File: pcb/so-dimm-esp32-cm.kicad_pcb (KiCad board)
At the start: 4 copper layers, 67.6 x 31.1 mm, 31 parts, among them IC1 PI4IOE5V9535LEX, IC2 PI4IOE5V9535LEX, J1 SODIMM-200, J2 Debug Connector/DNP, U1 ESP32-S2-SOLO

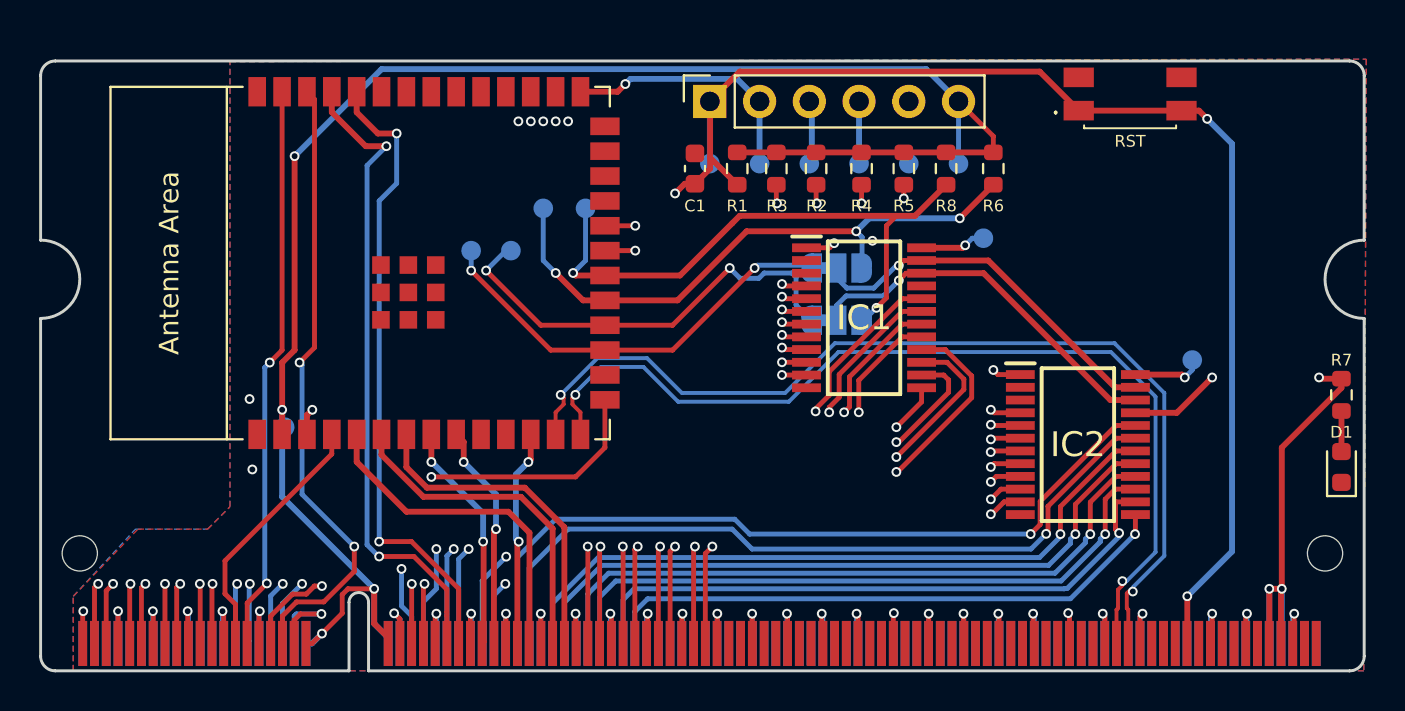
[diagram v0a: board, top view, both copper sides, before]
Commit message: Refactored PCB Layer to have one dedicated GND Layer + rerouted traces + removed debug connector and added IO0 to the SO-DIMM connector + added decoupling caps and delay circuit for ESP32 module
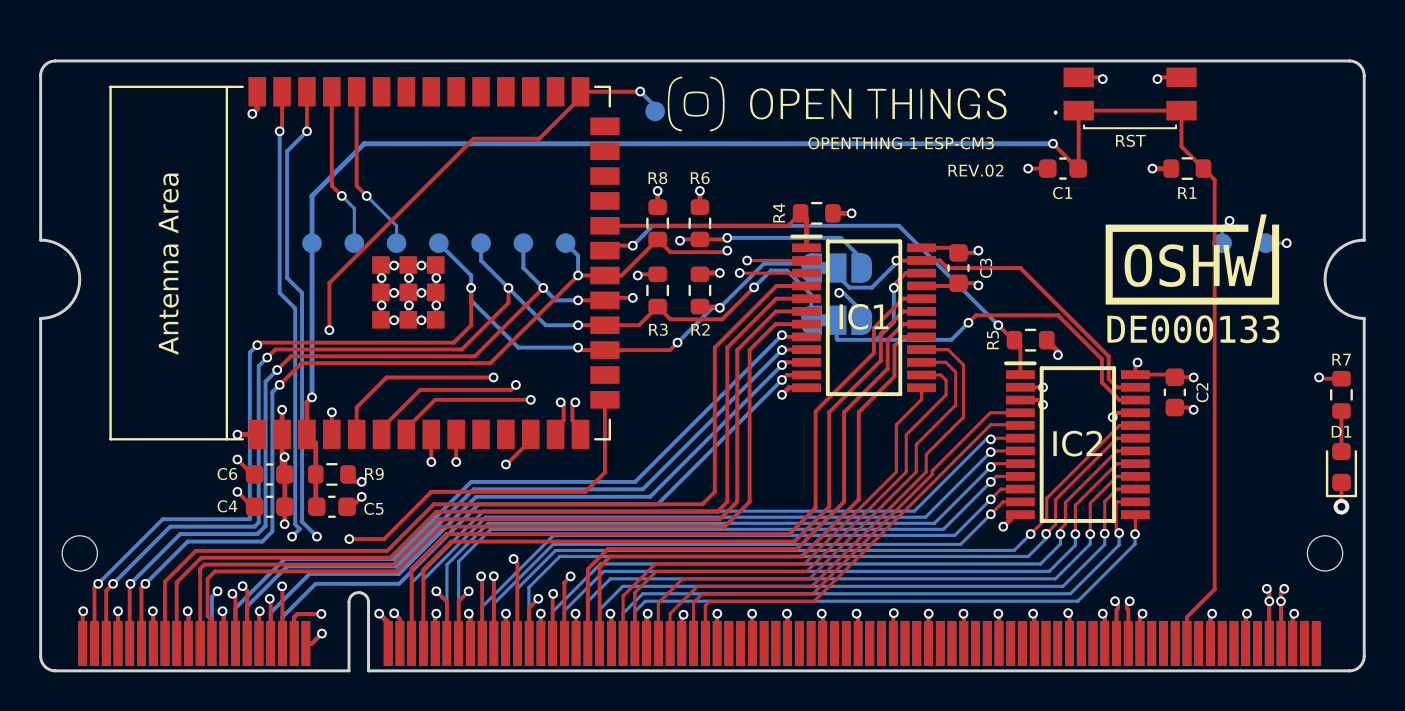
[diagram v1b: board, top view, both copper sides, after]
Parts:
- removed J2: Debug Connector/DNP, Connector_PinSocket_2.54mm:PinSocket_1x06_P2.54mm_Vertical
- removed TP5, TP7, TP9: TP_3V3, TestPoint:TestPoint_Pad_D1.0mm
- added C2: 0.1uF, Capacitor_SMD:C_0603_1608Metric, F.Cu at (173.4, 93.9)
- added C3: 0.1uF, Capacitor_SMD:C_0603_1608Metric, F.Cu at (162.3, 87.5)
- added C4: 10uF, Capacitor_SMD:C_0603_1608Metric, F.Cu at (127.1, 99.7)
- added C5: 1uF, Capacitor_SMD:C_0603_1608Metric, F.Cu at (130.3, 99.7)
- added C6: 0.1uF, Capacitor_SMD:C_0603_1608Metric, F.Cu at (127.1, 98.0)
- added G1: LOGO, LOGO, F.Cu at (156.3, 79.1)
- added G2: LOGO, LOGO, F.Cu at (174.2, 88.3)
- added R9: 10k, Resistor_SMD:R_0603_1608Metric, F.Cu at (130.3, 98.0)
- moved TP8 51.0 mm to (178.0, 86.2)
- moved TP4 26.1 mm to (131.4, 86.2)
- moved R1 23.0 mm to (174.0, 82.4), turned to 180 degrees
- moved TP3 21.5 mm to (133.6, 86.2)
- moved TP1 20.7 mm to (129.3, 86.2)
- moved C1 18.8 mm to (167.6, 82.4), turned to 180 degrees
- moved TP6 16.5 mm to (175.8, 86.2)
- moved R6 15.2 mm to (149.1, 85.2)
- moved R8 15.0 mm to (146.9, 85.2)
- moved R5 10.9 mm to (166.0, 91.2), turned to 0 degrees
- moved R3 8.69 mm to (146.9, 88.6)
- moved R2 8.60 mm to (149.1, 88.6)
- moved TP2 5.96 mm to (146.8, 79.5)
- moved R4 3.23 mm to (155.1, 84.7), turned to 0 degrees
- moved TP12 2.05 mm to (140.1, 86.2)
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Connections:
- J1 pad 24: unconnected-(J1-Pad24) -> /ESP32-CM/IO0
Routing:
- net +3V3: track 159.7 -> 41.4 mm, vias 10 -> 23
- net /ESP32-CM/IO0: track 13.1 -> 42.3 mm, vias 1 -> 3
- net /ESP32-CM/TXD0: track 61.4 -> 33.3 mm
- net /ESP32-CM/RXD0: track 57.6 -> 33.8 mm
- net GND: track 156.3 -> 142.0 mm, vias 39 -> 62
- net /ESP32-CM/USB_D+: track 48.8 -> 36.9 mm
- net /ESP32-CM/USB_D-: track 50.4 -> 38.5 mm
- net /SCL1: track 62.3 -> 55.1 mm, vias 3 -> 5
- net /ESP32-CM/V1SPI_MISO: track 17.4 -> 23.7 mm, vias 0 -> 2
- net /SDA1: track 62.4 -> 56.9 mm, vias 4 -> 7
- net /~{E1_INT}: track 17.2 -> 12.1 mm, vias 3 -> 0
- net E1_IO0_3: track 39.0 -> 43.9 mm, vias 2 -> 0
- net /ESP32-CM/V1SPI_MOSI: track 17.2 -> 22.1 mm, vias 0 -> 2
- net E1_IO0_2: track 39.9 -> 44.8 mm, vias 2 -> 0
- net /SCL: track 19.4 -> 24.1 mm, vias 1 -> 2
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- added copper zone on In2.Cu, net +3V3
- added copper zone on In1.Cu, net GND
- removed copper zone on B.Cu, net GND
- removed copper zone on F.Cu, net GND
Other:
- board text added: "OPENTHING 1 ESP-CM3"
- board text added: "REV.02"

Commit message: Fix missing ESP-SOLO footprint and Symbol
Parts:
- removed U1: ESP32-S2-SOLO, Espressif:ESP32-S2-SOLO
- added U2: ESP32-S2-SOLO, PCM_Espressif:ESP32-S2-SOLO, F.Cu at (134.8, 87.2)
- S1: footprint KiCad:EVQPUA02K -> EVQ-PUA02K:EVQPUA02K
